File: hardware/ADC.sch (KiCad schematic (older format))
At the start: 4 parts, among them U3 ADS1113/15

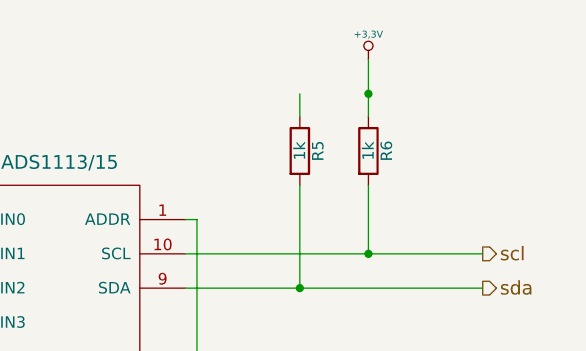
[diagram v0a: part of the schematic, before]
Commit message: Se finalizo esquematico del cricuito.
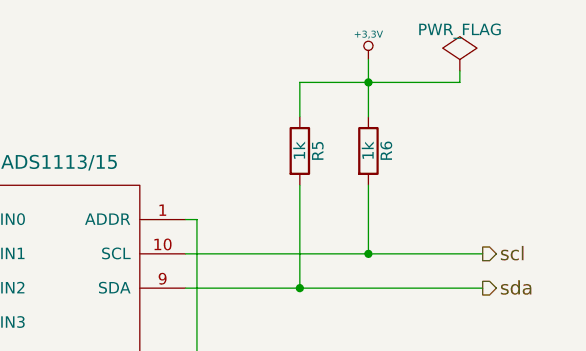
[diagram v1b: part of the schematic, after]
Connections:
- wire segments 14 -> 16
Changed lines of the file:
@@
 encoding utf-8
 Sheet 2 5
-Title ""
-Date ""
+Title "Diagrama de Conversor Analogo Digital."
+Date "2016-07-04"
 Rev ""
-Comp ""
+Comp "Felipe Rey"
 Comment1 ""
 Comment2 ""
@@
 $EndComp
 $Comp
-L GND #PWR?
+L GND #PWR01
 U 1 1 5785BB3C
 P 5800 4300
-F 0 "#PWR?" H 5800 4050 50  0001 C CNN
+F 0 "#PWR01" H 5800 4050 50  0001 C CNN
 F 1 "GND" H 5800 4150 50  0000 C CNN
 F 2 "" H 5800 4300 60  0000 C CNN
@@
 $EndComp
 $Comp
-L GND #PWR?
+L GND #PWR02
 U 1 1 5785BB54
 P 6150 4300
-F 0 "#PWR?" H 6150 4050 50  0001 C CNN
+F 0 "#PWR02" H 6150 4050 50  0001 C CNN
 F 1 "GND" H 6150 4150 50  0000 C CNN
 F 2 "" H 6150 4300 60  0000 C CNN
@@
 	6150 4200 6150 4300
 $Comp
-L +5V #PWR?
+L +5V #PWR03
 U 1 1 5785BB9C
 P 6150 3600
-F 0 "#PWR?" H 6150 3450 50  0001 C CNN
+F 0 "#PWR03" H 6150 3450 50  0001 C CNN
 F 1 "+5V" H 6150 3740 50  0000 C CNN
 F 2 "" H 6150 3600 60  0000 C CNN
@@
 $EndComp
 $Comp
-L +3,3V #PWR?
+L +3,3V #PWR04
 U 1 1 5785BF8D
 P 6550 2000
-F 0 "#PWR?" H 6550 1960 30  0001 C CNN
+F 0 "#PWR04" H 6550 1960 30  0001 C CNN
 F 1 "+3,3V" H 6550 2110 30  0000 C CNN
 F 2 "" H 6550 2000 60  0000 C CNN
@@
 	1    0    0    -1
 $EndComp
-Wire Wire Line
-	6550 2250 6550 2000
-Wire Wire Line
-	6250 2250 6250 2150
-Connection ~ 6550 2150
 Wire Wire Line
 	6550 2550 6550 2850
@@
 Wire Wire Line
 	5750 3350 7050 3350
+Wire Wire Line
+	6550 2250 6550 2000
+Wire Wire Line
+	6250 2250 6250 2100
+Wire Wire Line
+	6250 2100 6950 2100
+Connection ~ 6550 2100
+$Comp
+L PWR_FLAG #FLG05
+U 1 1 578E9319
+P 6950 2050
+F 0 "#FLG05" H 6950 2145 50  0001 C CNN
+F 1 "PWR_FLAG" H 6950 2230 50  0000 C CNN
+F 2 "" H 6950 2050 50  0000 C CNN
+F 3 "" H 6950 2050 50  0000 C CNN
+	1    6950 2050
+	1    0    0    -1
+$EndComp
+Wire Wire Line
+	6950 2100 6950 2050
 $EndSCHEMATC

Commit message: Se cargaron los footprint de los componentes.
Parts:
- C6: footprint (none) -> Capacitors_SMD:C_0805
- R5, R6: footprint (none) -> ej2cese:R_1206_HandSoldering
- U3: footprint (none) -> Housings_SSOP:MSOP-10_3x3mm_Pitch0.5mm
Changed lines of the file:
@@
 LIBS:valves
 LIBS:ej2cese
+LIBS:ADS1113IDGSR
 LIBS:poncho_celda-cache
 EELAYER 25 0
@@
 F 0 "U3" H 5200 2500 60  0000 C CNN
 F 1 "ADS1113/15" H 5200 4050 60  0000 C CNN
-F 2 "" H 5200 2500 60  0000 C CNN
+F 2 "Housings_SSOP:MSOP-10_3x3mm_Pitch0.5mm" H 5200 2500 60  0001 C CNN
 F 3 "http://www.ti.com/general/docs/lit/getliterature.tsp?genericPartNumber=ads1115&fileType=pdf" H 5200 2500 60  0001 C CNN
 	1    5250 3250
@@
 F 0 "C6" H 6175 4150 50  0000 L CNN
 F 1 "0.1uF" H 6175 3950 50  0000 L CNN
-F 2 "" H 6150 4050 60  0000 C CNN
+F 2 "Capacitors_SMD:C_0805" H 6150 4050 60  0001 C CNN
 F 3 "" H 6150 4050 60  0000 C CNN
 	1    6150 4050
@@
 F 0 "R6" V 6630 2400 50  0000 C CNN
 F 1 "1k" V 6550 2400 50  0000 C CNN
-F 2 "" V 6480 2400 30  0000 C CNN
+F 2 "ej2cese:R_1206_HandSoldering" V 6480 2400 30  0001 C CNN
 F 3 "" H 6550 2400 30  0000 C CNN
 	1    6550 2400
@@
 F 0 "R5" V 6330 2400 50  0000 C CNN
 F 1 "1k" V 6250 2400 50  0000 C CNN
-F 2 "" V 6180 2400 30  0000 C CNN
+F 2 "ej2cese:R_1206_HandSoldering" V 6180 2400 30  0001 C CNN
 F 3 "" H 6250 2400 30  0000 C CNN
 	1    6250 2400

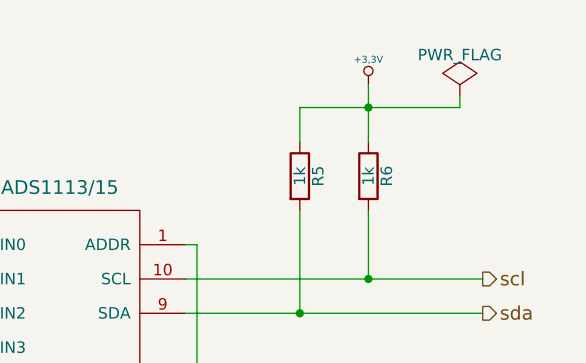
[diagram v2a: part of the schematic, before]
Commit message: Se realizo diseño de PCB doble capa.
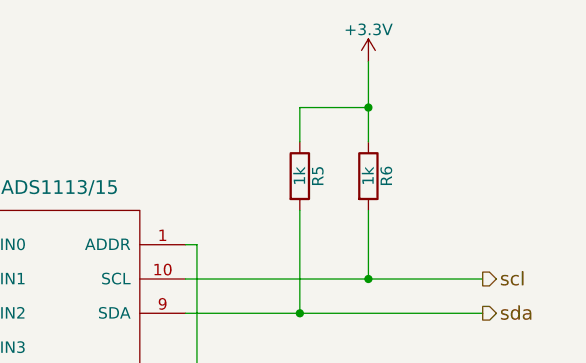
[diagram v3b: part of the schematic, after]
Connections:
- net +3.3V renamed +3V3
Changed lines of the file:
@@
-	1    0    0    -1
-$EndComp
-$Comp
-L +3,3V #PWR04
-U 1 1 5785BF8D
-P 6550 2000
-F 0 "#PWR04" H 6550 1960 30  0001 C CNN
-F 1 "+3,3V" H 6550 2110 30  0000 C CNN
-F 2 "" H 6550 2000 60  0000 C CNN
-F 3 "" H 6550 2000 60  0000 C CNN
-	1    6550 2000
 	1    0    0    -1
 $EndComp
@@
 	5750 3350 7050 3350
 Wire Wire Line
-	6550 2250 6550 2000
+	6550 1900 6550 2250
 Wire Wire Line
 	6250 2250 6250 2100
-Wire Wire Line
-	6250 2100 6950 2100
 Connection ~ 6550 2100
 $Comp
-L PWR_FLAG #FLG05
-U 1 1 578E9319
-P 6950 2050
-F 0 "#FLG05" H 6950 2145 50  0001 C CNN
-F 1 "PWR_FLAG" H 6950 2230 50  0000 C CNN
-F 2 "" H 6950 2050 50  0000 C CNN
-F 3 "" H 6950 2050 50  0000 C CNN
-	1    6950 2050
+L +3.3V #PWR05
+U 1 1 578EC5C8
+P 6550 1900
+F 0 "#PWR05" H 6550 1750 50  0001 C CNN
+F 1 "+3.3V" H 6550 2040 50  0000 C CNN
+F 2 "" H 6550 1900 50  0000 C CNN
+F 3 "" H 6550 1900 50  0000 C CNN
+	1    6550 1900
 	1    0    0    -1
 $EndComp
 Wire Wire Line
-	6950 2100 6950 2050
+	6250 2100 6550 2100
 $EndSCHEMATC
